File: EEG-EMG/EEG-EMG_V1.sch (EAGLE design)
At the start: 1 part

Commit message: Added 4 input stage amplifiers- AD8237
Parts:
- added BAT1: 2032, SMTU-2032-1:2032
- added C1, C10, C11, C2, C4, C5, C7, C8: 0.1uF, SparkFun-Capacitors:CAP0805
- added C12, C3, C6, C9: 1uF, SparkFun-Capacitors:CAP0805
- added IA_1, IA_2, IA_4: AD8237, wts_transmitter:AD8237
- added JP1: (no value), jumper:JP2W
- added JP2: (no value), jumper:JP2Q
- added R1, R10, R4, R7: 100k, SparkFun-Passives:RESISTOR0805-RES
- added R11, R2, R5, R8: 2k, SparkFun-Passives:RESISTOR0805-RES
- added R12, R3, R6, R9: 1k, SparkFun-Passives:RESISTOR0805-RES
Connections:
- new net EEG1+: IA_1.IN+, JP1.1
- new net EEG2+: IA_2.IN+, JP1.2
- new net EMG1+: IA_3.IN+, JP2.1
- new net EMG1-: IA_3.IN-, JP2.2
- new net EMG2+: IA_4.IN+, JP2.3
- new net EMG2-: IA_4.IN-, JP2.4
- new net GND: BAT1.-, C1.1, C10.1, C11.1, C12.2, C2.1, C3.2, C4.1, C5.1, C6.2, C7.1, C8.1, C9.2, IA_1.-VS, IA_2.-VS, IA_3.-VS, IA_4.-VS
- new net N$1: IA_1.VOUT, R1.1, R3.1
- new net N$10: IA_4.VOUT, R10.1, R12.1
- new net N$11: IA_4.FB, R10.2, R11.2
- new net N$12: C12.1, R12.2
- new net N$2: IA_1.FB, R1.2, R2.2
- new net N$3: C3.1, R3.2
- new net N$4: IA_2.VOUT, R4.1, R6.1
- new net N$5: IA_2.FB, R4.2, R5.2
- new net N$6: C6.1, R6.2
- new net N$7: IA_3.VOUT, R7.1, R9.1
- new net N$8: IA_3.FB, R7.2, R8.2
- new net N$9: C9.1, R9.2
- new net REF: IA_1.IN-, IA_2.IN-, JP1.3
- new net VAA: BAT1.+, C1.2, C10.2, C11.2, C2.2, C4.2, C5.2, C7.2, C8.2, IA_1.+VS, IA_1.BW, IA_2.+VS, IA_2.BW, IA_3.+VS, IA_3.BW, IA_4.+VS, IA_4.BW
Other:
- moved on the sheet: IA_3

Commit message: Added MCP6v31U
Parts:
- added C13, C14, C15, C16: 3.3uF, SparkFun-Capacitors:CAP0805
- added IC1, IC2, IC3, IC4: MCP6V31, linear:MCP601OT
- added R13, R14, R15, R16, R18, R19, R22, R23: 1M, SparkFun-Passives:RESISTOR0805-RES
- added R17, R20, R21, R24: 500k, SparkFun-Passives:RESISTOR0805-RES
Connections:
- new net N$13: C13.1, IC1.-IN, R14.2
- new net N$14: C13.2, IC1.OUT, R13.2
- new net N$16: C14.1, IC2.-IN, R15.1, R16.2
- new net N$17: C14.2, IC2.OUT, R15.2
- new net N$19: C15.1, IC3.-IN, R18.1, R19.2
- new net N$20: C15.2, IC3.OUT, R18.2
- new net N$22: C16.1, IC4.-IN, R23.2
- new net N$23: C16.2, IC4.OUT, R22.2
- net GND: now also IC1.V+, IC2.V+, IC3.V+, IC4.V+
- net N$2: now also R14.1
- net N$5: now also R16.1
- net N$8: now also R19.1
- net VAA: now also IC1.V-, IC2.V-, IC3.V-, IC4.V-

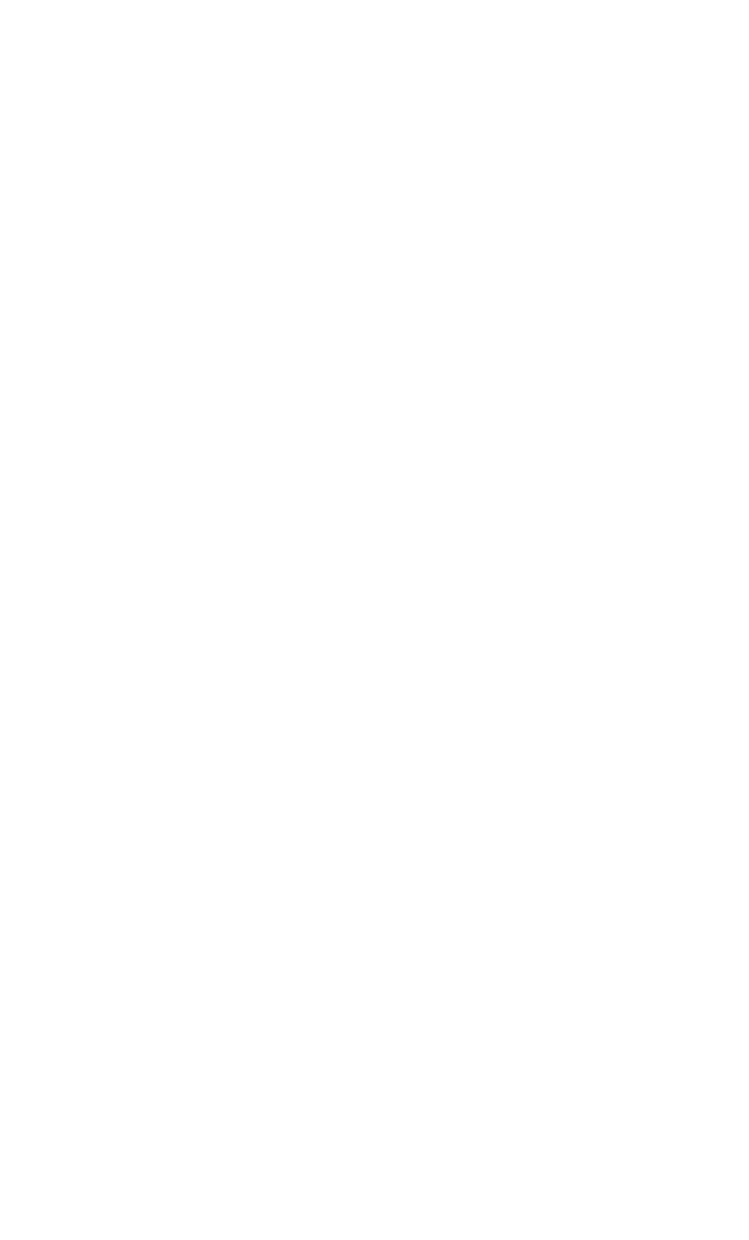
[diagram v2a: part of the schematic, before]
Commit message: Imported Components MCP3912 & LM7332MA
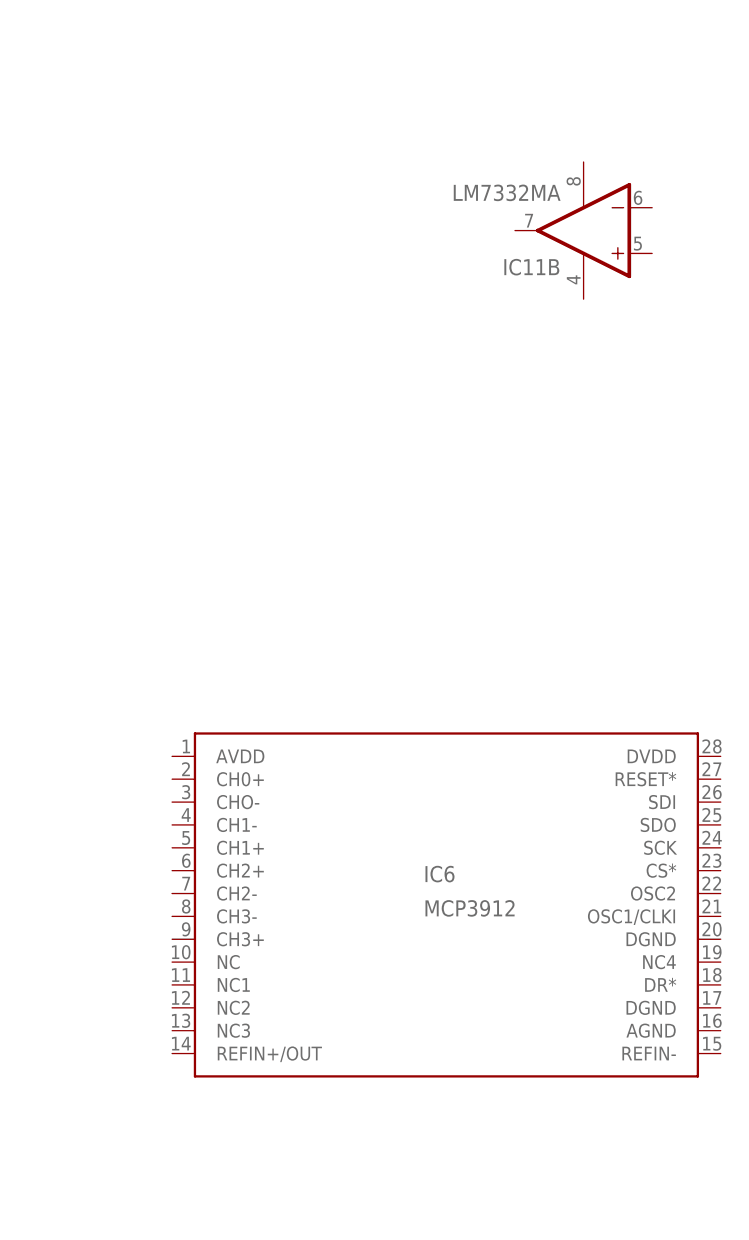
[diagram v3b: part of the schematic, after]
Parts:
- added IC11: LM7332MA, linear:LM1458D
- added IC6: MCP3912, SensorCape:MCP3912
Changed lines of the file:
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@@
 <part name="GND13" library="SparkFun-Aesthetics" deviceset="GND" device=""/>
 <part name="SUPPLY9" library="SparkFun-Aesthetics" deviceset="3.3V" device=""/>
+<part name="IC11" library="linear" deviceset="*1458" device="D" technology="LM" value="LM7332MA"/>
+<part name="IC6" library="SensorCape" deviceset="MCP3912" device=""/>
 </parts>
 <sheets>
@@
 </instance>
 <instance part="SUPPLY9" gate="G$1" x="647.7" y="-416.56" rot="R270"/>
+<instance part="IC11" gate="B" x="762" y="-149.86" rot="R180"/>
+<instance part="IC11" gate="P" x="762" y="-149.86"/>
+<instance part="IC6" gate="G$1" x="746.76" y="-223.52"/>
 </instances>
 <busses>

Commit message: Completed connections to all 4 Instrumentation Amplifiers
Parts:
- added C17: 0.1uF, SparkFun-Capacitors:CAP0805
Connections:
- new net N$15: C17.1, IC11B.+IN, IC6.REFIN+/OUT
- new net N$18: IC11B.-IN, IC11B.OUT, IC6.CH1-, IC6.CH2-, IC6.CH3-, IC6.CHO-, R11.1, R17.1, R2.1, R20.1, R21.1, R24.1, R5.1, R8.1
- new net N$21: IC2.+IN, R17.2
- new net N$24: IC3.+IN, R20.2
- new net N$25: IC1.+IN, R21.2
- new net N$26: IC4.+IN, R24.2
- net GND: now also C17.2, IC11P.V-
- net N$12: now also IC6.CH3+
- net N$14: now also IA_1.REF
- net N$17: now also IA_2.REF
- net N$20: now also IA_3.REF
- net N$23: now also IA_4.REF
- net N$3: now also IC6.CH0+
- net N$6: now also IC6.CH1+
- net VAA: now also IC11P.V+
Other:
- moved on the sheet: IC6

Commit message: Completed connections to MCP3912
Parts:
- added BAT2: 2032, SMTU-2032-1:2032
- added BATT: M02POLAR_LOCK, SparkFun-Connectors:M02POLAR_LOCK
- added C18, C45: 0.1uF, SparkFun-Capacitors:CAP0805
- added C19, C20: 18uF, SparkFun-Capacitors:CAP0805
- added C21, C22, C25, C28, C33, C37, C38: 0.1uF, resistor:C-EUC1206
- added C23, C31, C43: 10uF, resistor:C-EUC1206
- added C24, C26, C27, C39, C40: 1uF, resistor:C-EUC1206
- added C29, C30, C41, C42: 18pF, resistor:C-EUC1206
- added C32: 100nF, resistor:C-EUC1206
- added C34, C35: 4.7uF, resistor:C-EUC1206
- added C36, C44: 47 uF, resistor:C-EUC1206
- added CONN1: ANALOG, adafruit:PINHD-1X6B
- added CONN2: DIGITAL, adafruit:PINHD-1X8BIG
- added CONN3: DIGITAL, adafruit:PINHD-1X10
- added CONN4: DIGITAL RASTER, adafruit:PINHD-1X10
- added CONN5: POWER, adafruit:PINHD-1X6B
- added D13, D13_2, RX, RX1, TX, TX1: Green, SparkFun-LED:LED1206
- added D3: B330A, aaron_discrete:B330A
- added D4: POWER, SparkFun-LED:LED1206
- added F1, F2: 1206L, microbuilder:PTC1206_L
- added FET1, FET3: TR, aaron_discrete:IRLML2502TR
- added JP3, JP4: ISP, SparkFun:AVR_SPI_PRG_6PTH
- added JP5, JP6: (no value), SparkFun-Connectors:M03X22X3_SILK_SM
- added L1: Ferrite, wuerth-elektronik:WE-CBF_1206W
- added L2: BRL3225T3R3M, resistor:L-EUL3225P
- added MINIUSB, MINIUSB1: MINI-USB-SCHIELD-32005-201, con-cypressindustries:MINI-USB-SCHIELD-32005-201
- added MUX: 74HC4051, SparkFun-AnalogIC:74HC4051_MUX
- added Q1, Q6, Q7: CSM-3X-CRYSTALCSM-3X, fmc:CSM-3X-CRYSTALCSM-3X
- added Q2, Q3, Q4, Q5: QRE1113, aaron_discrete:QRE1113
- added R25, R31, R33, R35, R37, R39, R47, R48: 10K, resistor:R-EU_R1206
- added R26, R29, R30, R43, R44, R45, R51: 1K, resistor:R-EU_R1206
- added R27, R28, R50, R52: 22, resistor:R-EU_R1206
- added R32, R34, R36, R38, R40, R46: 100, resistor:R-EU_R1206
- added R41: 470, resistor:R-EU_R1206
- added R42: 2K, resistor:R-EU_R1206
- added R49: 3.09k, resistor:R-EU_R1206
- added R53, R54: 2.2K, resistor:R-EU_R1206
- added S1, S2: Reset, SparkFun:TAC_SWITCHSMD
- added SERVO1(USONIC): USONIC, pinhead:PINHD-1X3
- added SERVO2(GRIP): GRIPPER, pinhead:PINHD-1X3
- added SERVO3(GRIPROT): ROTATE, pinhead:PINHD-1X3
- added SER_CPU2: SER2, pinhead:PINHD-1X2
- added SHIFT1, SHIFT2: 74HC595D, 74xx-eu:74HC595D
- added STEPPER_DRIVER: ULN2803, SparkFun-PowerIC:ULN2803SOICW
- added SW1: (no value), switch:SPDT
- added U$10: PNA460XM, adafruit:PNA460XM
- added U$2: 1.8TFT+SD, muzy_robot:1.8TFT+SD
- added U$3: GY-521, muzy_robot:GY-521
- added U$4: HMC5883L, muzy_robot:HMC5883L
- added U$5: NRF24L01+, muzy_robot:NRF24L01+
- added U1: USER, adafruit:ATMEGA32U4-AU
- added U2: BRAIN, adafruit:ATMEGA32U4-AU
- added U3: LP2985, SparkFun:V_REG_LDOSMD
- added U4: MCP1650, aaron_ic:MCP1650
- added U5: MCP73831, SparkFun:MCP73831SMD
- added ULTRASONIC: (no value), pinhead:PINHD-1X4
- added X1, X2: 05-JST-B5B-XH-A, con-jst-xh:05-JST-B5B-XH-A
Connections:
- removed net VAA: BAT1.+, C1.2, C10.2, C11.2, C2.2, C4.2, C5.2, C7.2, C8.2, IA_1.+VS, IA_1.BW, IA_2.+VS, IA_2.BW, IA_3.+VS, IA_3.BW, IA_4.+VS, IA_4.BW, IC1.V-, IC11P.V+, IC2.V-, IC3.V-, IC4.V-
- new net 2D+: R50.1, U2.D+
- new net 2D-: R52.1, U2.D-
- new net 2D13: R43.1, U2.PC7(ICP3/CLK0/OC4A)
- new net 2MISO: JP4.1, U$2.SD_MISO, U$5.MISO, U2.PB3(PDO/MISO)
- new net 2MOSI: JP4.4, SHIFT1A.SER, U$2.SDA, U$2.SD_MOSI, U$5.MOSI, U2.PB2(PDI/MISO)
- new net 2RESET: JP4.5, R47.1, S1.3, S1.4, U2./RESET
- new net 2RXLED: R44.1, U2.PB0(SS)
- new net 2SCK: JP4.3, SHIFT1A.SCK, SHIFT2A.SCK, U$2.SCK, U$2.SD_SCK, U$5.SCK, U2.PB1(SCK)
- new net 2TXLED: R45.1, U2.PD5(XCK/CTS)
- new net 2XTAL3: C42.1, Q6.2, U2.XTAL2
- new net 2XTAL4: C41.1, Q6.1, U2.XTAL1
- new net 3.3V: C31.1, C32.1, CONN5.2, U$2.LED, U$5.VCC, U3.OUT
- new net A0: CONN1.1, U1.PF7(ADC7(TDI)
- new net A1: CONN1.2, U1.PF6(ADC6/TDO)
- new net A2: CONN1.3, U1.PF5(ADC5/TMS)
- new net A3: CONN1.4, U1.PF4(ADC4/TCK)
- new net A4: CONN1.5, U1.PF1(ADC1)
- new net A5: CONN1.6, U1.PF0(ADC0)
- new net AREF: C22.2, C38.2, CONN3.8, CONN4.8, U1.AREF, U2.AREF
- new net AVCC: C25.1, C28.1, L1.2, U1.AVCC, U1.AVCC1, U2.AVCC, U2.AVCC1
- new net BATT_OUT: C44.1, D3.C, R46.2, R49.2, SW1.1
- new net D+: R27.1, U1.D+
- new net D-: R28.1, U1.D-
- new net D10: CONN3.3, CONN4.3, U1.PB6(OC1B/OC4B/ADC13)
- new net D11: CONN3.4, CONN4.4, U1.PB7(OC0A/OC1C/RTS)
- new net D12: CONN3.5, CONN4.5, U1.PD6(T1/OC4D/ADC9)
- new net D13: CONN3.6, CONN4.6, R26.1, U1.PC7(ICP3/CLK0/OC4A)
- new net D4: CONN2.5, U1.PD4(ICP1/ADC8)
- new net D5: CONN2.6, U1.PC6(OC1A)
- new net D6: CONN2.7, U1.PD7(OC4D/ADC10/T0)
- new net D7: CONN2.8, U1.PE6
- new net D8: CONN3.1, CONN4.1, U1.PB4(ADC11)
- new net D9: CONN3.2, CONN4.2, U1.PB5(OC1A/OC4B/ADC12)
- new net ECHO: U2.PF6(ADC6/TDO), ULTRASONIC.2
- new net IR: U$10.OUT, U2.PD4(ICP1/ADC8)
- new net IRA: JP6.1, MUX.A
- new net IRB: JP6.3, MUX.B
- new net IRC: JP6.5, MUX.C
- new net IR_GND: JP6.6, MUX.INH, MUX.VEE, MUX.VSS, Q2.E, Q2.K, Q3.E, Q3.K, Q4.E, Q4.K, Q5.E, Q5.K
- new net IR_OUT: JP6.4, MUX.IO
- new net IR_VCC: JP6.2, MUX.VDD, R32.2, R33.2, R34.2, R35.2, R36.2, R37.2, R38.2, R39.2
- new net MISO: JP3.1, U1.PB3(PDO/MISO)
- new net MOSI: JP3.4, U1.PB2(PDI/MISO)
- new net MUX0: MUX.IO0, Q2.C, R33.1
- new net MUX1: MUX.IO1, Q3.C, R35.1
- new net MUX2: MUX.IO2, Q4.C, R37.1
- new net MUX3: MUX.IO3, Q5.C, R39.1
- new net MUX_OUT: JP5.4, U2.PF0(ADC0)
- new net N$134: C19.2, IC6.OSC1/CLKI, Q7.1
- new net N$135: C20.2, IC6.OSC2, Q7.2
- new net N$136: D13.A, R26.2
- new net N$137: R31.1, U1.PE2(HWB)
- new net N$138: F2.1, MINIUSBG$1.1
- new net N$139: R30.2, TX.C
- new net N$140: R29.2, RX.C
- new net N$141: MINIUSBG$1.2, R28.2
- new net N$142: MINIUSBG$1.3, R27.2
- new net N$143: Q2.A, R32.1
- new net N$144: Q3.A, R34.1
- new net N$145: Q4.A, R36.1
- new net N$146: Q5.A, R38.1
- new net N$147: FET1.G, R40.2
- new net N$148: R49.1, R51.2, U4.FB
- new net N$149: C33.1, R46.1, U4./SHDN, U4.CS, U4.VIN
- new net N$150: FET3.G, U4.EXT
- new net N$151: D3.A, FET3.D, L2.2
- new net N$152: R42.1, U5.PROG
- new net N$153: R41.1, U5.STAT
- new net N$154: D4.C, R41.2
- new net N$155: STEPPER_DRIVER.11, X2-4.1
- new net N$156: STEPPER_DRIVER.12, X2-3.1
- new net N$157: STEPPER_DRIVER.13, X2-2.1
- new net N$158: STEPPER_DRIVER.14, X2-1.1
- new net N$159: STEPPER_DRIVER.15, X1-4.1
- new net N$160: STEPPER_DRIVER.16, X1-3.1
- new net N$161: STEPPER_DRIVER.17, X1-2.1
- new net N$162: STEPPER_DRIVER.18, X1-1.1
- new net N$163: D13_2.A, R43.2
- new net N$164: R45.2, TX1.C
- new net N$165: R44.2, RX1.C
- new net N$166: R48.1, U2.PE2(HWB)
- new net N$167: F1.1, MINIUSB1G$1.1
- new net N$168: MINIUSB1G$1.2, R52.2
- new net N$169: MINIUSB1G$1.3, R50.2
- new net N$170: SER_CPU2.1, U2.PD3(INT3/TXD1)
- new net N$171: SER_CPU2.2, U2.PD2(INT2/RXD1)
- new net N$172: C39.1, U2.UCAP
- new net N$173: C26.1, U1.UCAP
- new net N$174: JP5.1, SHIFT2A.QA
- new net N$175: JP5.3, SHIFT2A.QB
- new net N$176: JP5.5, SHIFT2A.QC
- new net N$177: FET1.D, JP5.6
- new net NRF_CE: U$5.CE, U2.PB5(OC1A/OC4B/ADC12)
- new net NRF_CSN: U$5.CSN, U2.PB6(OC1B/OC4B/ADC13)
- new net NRF_IRQ: U$5.IRQ, U2.PE6
- new net RESET: CONN5.1, JP3.5, R25.1, S2.3, S2.4, U1./RESET
- new net RX-I: CONN2.1, U1.PD2(INT2/RXD1)
- new net RXLED: R29.1, U1.PB0(SS)
- new net S1: SHIFT1A.QA, STEPPER_DRIVER.8
- new net S1OVERFLOW1: SHIFT1A.QH*, SHIFT2A.SER
- new net S2: SHIFT1A.QB, STEPPER_DRIVER.7
- new net S2O4: R40.1, SHIFT2A.QD
- new net S3: SHIFT1A.QC, STEPPER_DRIVER.6
- new net S4: SHIFT1A.QD, STEPPER_DRIVER.5
- new net S5: SHIFT1A.QE, STEPPER_DRIVER.4
- new net S6: SHIFT1A.QF, STEPPER_DRIVER.3
- new net S7: SHIFT1A.QG, STEPPER_DRIVER.2
- new net S8: SHIFT1A.QH, STEPPER_DRIVER.1
- new net SCK: JP3.3, U1.PB1(SCK)
- new net SCL: CONN2.4, CONN3.10, CONN4.10, R53.1, U$3.SCL, U$4.SCL, U1.PD0(INT0/OC0B), U2.PD0(INT0/OC0B)
- new net SDA: CONN2.3, CONN3.9, CONN4.9, R54.1, U$3.SDA, U$4.SDA, U1.PD1(INT1/SDA), U2.PD1(INT1/SDA)
- new net SD_CS: U$2.SD_CS, U2.PB4(ADC11)
- new net SHIFT_RCK: SHIFT1A.RCK, SHIFT2A.RCK, U2.PD6(T1/OC4D/ADC9)
- new net S_GRIP: SERVO2(GRIP).3, U2.PD7(OC4D/ADC10/T0)
- new net S_GRIPROT: SERVO3(GRIPROT).3, U2.PB7(OC0A/OC1C/RTS)
- new net S_USONIC: SERVO1(USONIC).3, U2.PC6(OC1A)
- new net TFT_CS: U$2.CS, U2.PF1(ADC1)
- new net TFT_DC: U$2.AD, U2.PF5(ADC5/TMS)
- new net TFT_RST: U$2.RESET, U2.PF4(ADC4/TCK)
- new net TRIG: U2.PF7(ADC7(TDI), ULTRASONIC.3
- new net TX-O: CONN2.2, U1.PD3(INT3/TXD1)
- new net TXLED: R30.1, U1.PD5(XCK/CTS)
- new net USB_VIN: C23.1, C34.1, C43.1, D4.A, F1.2, F2.2, SW1.3, U5.VIN
- new net VBATT: BATT.2, C35.1, C36.2, L2.1, U5.VBAT
- new net VCC: C21.1, C24.1, C27.1, C37.1, C40.1, CONN5.3, JP3.2, JP4.2, JP5.2, L1.1, R25.2, R47.2, R53.2, R54.2, RX.A, RX1.A, SERVO1(USONIC).2, SERVO2(GRIP).2, SERVO3(GRIPROT).2, SHIFT1A.SCL, SHIFT1P.VCC, SHIFT2A.SCL, SHIFT2P.VCC, STEPPER_DRIVER.10, SW1.2, TX.A, TX1.A, U$10.VCC, U$2.VCC, U$3.VCC, U$4.VCC, U1.UVCC, U1.VBUS, U1.VCC, U1.VCC1, U2.UVCC, U2.VBUS, U2.VCC, U2.VCC1, U3.EN, U3.IN, ULTRASONIC.4, X1-5.1, X2-5.1
- new net VDD: BAT1.+, BAT2.+, C1.2, C10.2, C11.2, C18.2, C2.2, C4.2, C45.2, C5.2, C7.2, C8.2, IA_1.+VS, IA_1.BW, IA_2.+VS, IA_2.BW, IA_3.+VS, IA_3.BW, IA_4.+VS, IA_4.BW, IC1.V-, IC11P.V+, IC2.V-, IC3.V-, IC4.V-, IC6.AVDD, IC6.DVDD
- new net XTAL3: C30.1, Q1.2, U1.XTAL2
- new net XTAL4: C29.1, Q1.1, U1.XTAL1
- net GND: now also BAT2.-, BATT.1, C18.1, C19.1, C20.1, C21.2, C22.1, C23.2, C24.2, C25.2, C26.2, C27.2, C28.2, C29.2, C30.2, C31.2, C32.2, C33.2, C34.2, C35.2, C36.1, C37.2, C38.1, C39.2, C40.2, C41.2, C42.2, C43.2, C44.2, C45.1, CONN3.7, CONN4.7, CONN5.4, CONN5.5, D13.C, D13_2.C, FET1.S, FET3.S, IC6.AGND, IC6.DGND, IC6.DGND@1, IC6.NC, IC6.NC1, IC6.NC2, IC6.NC3, IC6.NC4, IC6.REFIN-, JP3.6, JP4.6, MINIUSB1G$1.5, MINIUSB1S.S1, MINIUSB1S.S2, MINIUSB1S.S3, MINIUSB1S.S4, MINIUSBG$1.5, MINIUSBS.S1, MINIUSBS.S2, MINIUSBS.S3, MINIUSBS.S4, R31.2, R42.2, R48.2, R51.1, S1.1, S1.2, S2.1, S2.2, SERVO1(USONIC).1, SERVO2(GRIP).1, SERVO3(GRIPROT).1, SHIFT1A.G, SHIFT1P.GND, SHIFT2A.G, SHIFT2P.GND, STEPPER_DRIVER.9, U$10.GND, U$2.GND, U$3.GND, U$4.GND, U$5.GND, U1.GND, U1.GND1, U1.GND2, U1.GND3, U1.UGND, U2.GND, U2.GND1, U2.GND2, U2.GND3, U2.UGND, U3.GND, U4.GND, U5.VSS, ULTRASONIC.1
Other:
- note added: "1.8" SPI Display (128*160px)"
- note added: "3.3V LDO"
- note added: "38KHz with digital output"
- note added: "Accelerometer and Gyroscope (GY-521, optional, plug-in module)"
- note added: "Analog Supply (CPU 1 and CPU 2)"
- note added: "Arduino Breakouts (CPU 1)"
- note added: "CPU 1 (ATMEGA32U4)"
- note added: "CPU 2 (ATMEGA32U4)"
- note added: "Compass (optional, plug-in module)"
- note added: "Edubot V.0.12 by Sebastian Muszytowski <muzy@muzy.eu>"
- note added: "GRIP mechanism servo"
- note added: "HC-SR04"
- note added: "HMC5883L"
- note added: "I2C Pullup"
- note added: "IR Reciever"
- note added: "ISP (CPU1)"
- note added: "ISP (CPU2)"
- note added: "Infrared Sensors (for Line Following)"
- note added: "Left Motor"
- note added: "LiPo Charge Circuit (PROG = 2K = 500mA)"
- note added: "MPU 6050"
- note added: "NO SUPPORT FOR VIN DUE TO MISSING REGULATOR. EVERYTHING ABOVE 5.5V DAMAGES THE BOARD!"
- note added: "NRF24L01 Breakout"
- note added: "Power Selector"
- note added: "ROTATE mechanism servo"
- note added: "Reset (CPU1)"
- note added: "Reset (CPU2)"
- note added: "Right Motor"
- note added: "Servo 1 (Ultrasonic)"
- note added: "Servo 2 and 3 (Gripper)"
- note added: "Shift Register and Mulitplexer (CPU 2)"
- note added: "Status LEDs (CPU1)"
- note added: "Status LEDs (CPU2)"
- note added: "Step-Up-Converter (2.8 to 4.2Volt to 5V @ 1A)"
- note added: "USB (CPU1)"
- note added: "USB (CPU2)"
- note added: "Ultrasonic distance sensor"
- note added: "based on Vinciduino Schematic and ATmega32U4 data sheet; Arduino Leonardo compatible with Headers The user mainly programs this microcontroller."
- note added: "based on Vinciduino Schematic and ATmega32U4 data sheet; Arduino Leonardo compatible without Headers This microcontroller serves as the "brain" interfacing internal components."
- note added: "for moving the Ultrasonic distance sensor to scan the environment"
- note added: "licensed under CC-BY-SA 3.0, based on the beautiful Vinciduino (vinciduino.org), inspired by Sparki (arcbotics.com), made with the lovely Arduino Leonardo in mind (arduino.cc)"
- note added: "on 2x4pin header pinout"
- note added: "optional, only populate when no other component provides pullup resistors! Values may vary (from 2.2K to 10K)"
- note added: "with SD Card Adapter (optional, plug-in module)"

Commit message: Added Bluetooth Module BGM111
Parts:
- removed BATT: M02POLAR_LOCK, SparkFun-Connectors:M02POLAR_LOCK
- removed C28, C33, C37, C38: 0.1uF, resistor:C-EUC1206
- removed C29, C30, C41, C42: 18pF, resistor:C-EUC1206
- removed C31, C43: 10uF, resistor:C-EUC1206
- removed C32: 100nF, resistor:C-EUC1206
- removed C34, C35: 4.7uF, resistor:C-EUC1206
- removed C36, C44: 47 uF, resistor:C-EUC1206
- removed C39, C40: 1uF, resistor:C-EUC1206
- removed CONN1: ANALOG, adafruit:PINHD-1X6B
- removed CONN2: DIGITAL, adafruit:PINHD-1X8BIG
- removed CONN3: DIGITAL, adafruit:PINHD-1X10
- removed CONN4: DIGITAL RASTER, adafruit:PINHD-1X10
- removed CONN5: POWER, adafruit:PINHD-1X6B
- removed D13, D13_2, RX, RX1, TX, TX1: Green, SparkFun-LED:LED1206
- removed D3: B330A, aaron_discrete:B330A
- removed D4: POWER, SparkFun-LED:LED1206
- removed F1, F2: 1206L, microbuilder:PTC1206_L
- removed FET1, FET3: TR, aaron_discrete:IRLML2502TR
- removed JP5, JP6: (no value), SparkFun-Connectors:M03X22X3_SILK_SM
- removed L1: Ferrite, wuerth-elektronik:WE-CBF_1206W
- removed L2: BRL3225T3R3M, resistor:L-EUL3225P
- removed MINIUSB, MINIUSB1: MINI-USB-SCHIELD-32005-201, con-cypressindustries:MINI-USB-SCHIELD-32005-201
- removed MUX: 74HC4051, SparkFun-AnalogIC:74HC4051_MUX
- removed Q1, Q6: CSM-3X-CRYSTALCSM-3X, fmc:CSM-3X-CRYSTALCSM-3X
- removed Q2, Q3, Q4, Q5: QRE1113, aaron_discrete:QRE1113
- removed R43, R44, R45, R51: 1K, resistor:R-EU_R1206
- removed R46: 100, resistor:R-EU_R1206
- removed R47, R48: 10K, resistor:R-EU_R1206
- removed R49: 3.09k, resistor:R-EU_R1206
- removed R50, R52: 22, resistor:R-EU_R1206
- removed R53, R54: 2.2K, resistor:R-EU_R1206
- removed S1, S2: Reset, SparkFun:TAC_SWITCHSMD
- removed SERVO1(USONIC): USONIC, pinhead:PINHD-1X3
- removed SERVO2(GRIP): GRIPPER, pinhead:PINHD-1X3
- removed SERVO3(GRIPROT): ROTATE, pinhead:PINHD-1X3
- removed SER_CPU2: SER2, pinhead:PINHD-1X2
- removed SHIFT1, SHIFT2: 74HC595D, 74xx-eu:74HC595D
- removed STEPPER_DRIVER: ULN2803, SparkFun-PowerIC:ULN2803SOICW
- removed SW1: (no value), switch:SPDT
- removed U$10: PNA460XM, adafruit:PNA460XM
- removed U$2: 1.8TFT+SD, muzy_robot:1.8TFT+SD
- removed U$3: GY-521, muzy_robot:GY-521
- removed U$4: HMC5883L, muzy_robot:HMC5883L
- removed U$5: NRF24L01+, muzy_robot:NRF24L01+
- removed U3: LP2985, SparkFun:V_REG_LDOSMD
- removed U5: MCP73831, SparkFun:MCP73831SMD
- removed ULTRASONIC: (no value), pinhead:PINHD-1X4
- removed X1, X2: 05-JST-B5B-XH-A, con-jst-xh:05-JST-B5B-XH-A
- added BAT3: 2032, SMTU-2032-1:2032
- added J1, J2: (no value), tag-connect:TC2030-MCP-NL
- added LOGO3: OSHW-LOGOS, SparkFun-Aesthetics:OSHW-LOGOS
- C21: value 0.1uF -> 1nF; device resistor:C-EUC1206 -> SparkFun-Passives:CAP0603-CAP
- C22: value 0.1uF -> 0.1uf; device resistor:C-EUC1206 -> SparkFun-Passives:CAP0603-CAP
- C23: value 10uF -> 0.1uF; device resistor:C-EUC1206 -> SparkFun-Passives:CAP0603-CAP
- C24: value 1uF -> 0.33uF; device resistor:C-EUC1206 -> SparkFun-Passives:CAP0805
- C25: value 0.1uF -> 0.33uF; device resistor:C-EUC1206 -> SparkFun-Passives:CAP0805
- C26: value 1uF -> 1.5nF; device resistor:C-EUC1206 -> SparkFun-Passives:CAP0603-CAP
- C27: value 1uF -> 10nF; device resistor:C-EUC1206 -> SparkFun-Passives:CAP0603-CAP
- JP3, JP4: value ISP -> SEWTAP2; device SparkFun:AVR_SPI_PRG_6PTH -> LilyPad-Wearables:SEWTAP2
- R25: value 10K -> 180k; device resistor:R-EU_R1206 -> SparkFun-Passives:RESISTOR0603-RES
- R26: value 1K -> 180k; device resistor:R-EU_R1206 -> SparkFun-Passives:RESISTOR0603-RES
- R27: value 22 -> 1M; device resistor:R-EU_R1206 -> SparkFun-Passives:RESISTOR0603-RES
- R28: value 22 -> 10M; device resistor:R-EU_R1206 -> SparkFun-Passives:RESISTOR0603-RES
- R29: value 1K -> 10M; device resistor:R-EU_R1206 -> SparkFun-Passives:RESISTOR0603-RES
- R30: value 1K -> 1M; device resistor:R-EU_R1206 -> SparkFun-Passives:RESISTOR0603-RES
- R31: value 10K -> 100k; device resistor:R-EU_R1206 -> SparkFun-Passives:RESISTOR0603-RES
- R32, R36: value 100 -> 10M; device resistor:R-EU_R1206 -> SparkFun-Passives:RESISTOR0603-RES
- R33, R35: value 10K -> 10M; device resistor:R-EU_R1206 -> SparkFun-Passives:RESISTOR0603-RES
- R34: value 100 -> 1.4M; device resistor:R-EU_R1206 -> SparkFun-Passives:RESISTOR0603-RES
- R37: value 10K -> 1M; device resistor:R-EU_R1206 -> SparkFun-Passives:RESISTOR0603-RES
- R38: value 100 -> 360k; device resistor:R-EU_R1206 -> SparkFun-Passives:RESISTOR0603-RES
- R39: value 10K -> 0; device resistor:R-EU_R1206 -> SparkFun-Resistors:0OHM1/10W5%(0603)
- R40: value 100 -> DNP; device resistor:R-EU_R1206 -> SparkFun-Resistors:0OHM1/10W5%(0603)
- R41: value 470 -> 0; device resistor:R-EU_R1206 -> SparkFun-Resistors:0OHM1/10W5%(0603)
- R42: value 2K -> DNP; device resistor:R-EU_R1206 -> SparkFun-Resistors:0OHM1/10W5%(0603)
- U1: value USER -> AD8232; device adafruit:ATMEGA32U4-AU -> AD8232:AD8232
- U2: value BRAIN -> BGM111-VISUAL-A; device adafruit:ATMEGA32U4-AU -> sf-bluegiga:BGM111-VISUAL-A
- U4: value MCP1650 -> BGM111-VISUAL-A; device aaron_ic:MCP1650 -> sf-bluegiga:BGM111-VISUAL-A
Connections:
- removed net 2D+: R50.1, U2.D+
- removed net 2D-: R52.1, U2.D-
- removed net 2D13: R43.1, U2.PC7(ICP3/CLK0/OC4A)
- removed net 2MISO: JP4.1, U$2.SD_MISO, U$5.MISO, U2.PB3(PDO/MISO)
- removed net 2MOSI: JP4.4, SHIFT1A.SER, U$2.SDA, U$2.SD_MOSI, U$5.MOSI, U2.PB2(PDI/MISO)
- removed net 2RESET: JP4.5, R47.1, S1.3, S1.4, U2./RESET
- removed net 2RXLED: R44.1, U2.PB0(SS)
- removed net 2SCK: JP4.3, SHIFT1A.SCK, SHIFT2A.SCK, U$2.SCK, U$2.SD_SCK, U$5.SCK, U2.PB1(SCK)
- removed net 2TXLED: R45.1, U2.PD5(XCK/CTS)
- removed net 2XTAL3: C42.1, Q6.2, U2.XTAL2
- removed net 2XTAL4: C41.1, Q6.1, U2.XTAL1
- removed net A0: CONN1.1, U1.PF7(ADC7(TDI)
- removed net A1: CONN1.2, U1.PF6(ADC6/TDO)
- removed net A2: CONN1.3, U1.PF5(ADC5/TMS)
- removed net A3: CONN1.4, U1.PF4(ADC4/TCK)
- removed net A4: CONN1.5, U1.PF1(ADC1)
- removed net A5: CONN1.6, U1.PF0(ADC0)
- removed net AREF: C22.2, C38.2, CONN3.8, CONN4.8, U1.AREF, U2.AREF
- removed net AVCC: C25.1, C28.1, L1.2, U1.AVCC, U1.AVCC1, U2.AVCC, U2.AVCC1
- removed net BATT_OUT: C44.1, D3.C, R46.2, R49.2, SW1.1
- removed net D+: R27.1, U1.D+
- removed net D-: R28.1, U1.D-
- removed net D10: CONN3.3, CONN4.3, U1.PB6(OC1B/OC4B/ADC13)
- removed net D11: CONN3.4, CONN4.4, U1.PB7(OC0A/OC1C/RTS)
- removed net D12: CONN3.5, CONN4.5, U1.PD6(T1/OC4D/ADC9)
- removed net D13: CONN3.6, CONN4.6, R26.1, U1.PC7(ICP3/CLK0/OC4A)
- removed net D4: CONN2.5, U1.PD4(ICP1/ADC8)
- removed net D5: CONN2.6, U1.PC6(OC1A)
- removed net D6: CONN2.7, U1.PD7(OC4D/ADC10/T0)
- removed net D7: CONN2.8, U1.PE6
- removed net D8: CONN3.1, CONN4.1, U1.PB4(ADC11)
- removed net D9: CONN3.2, CONN4.2, U1.PB5(OC1A/OC4B/ADC12)
- removed net ECHO: U2.PF6(ADC6/TDO), ULTRASONIC.2
- removed net IR: U$10.OUT, U2.PD4(ICP1/ADC8)
- removed net IRA: JP6.1, MUX.A
- removed net IRB: JP6.3, MUX.B
- removed net IRC: JP6.5, MUX.C
- removed net IR_GND: JP6.6, MUX.INH, MUX.VEE, MUX.VSS, Q2.E, Q2.K, Q3.E, Q3.K, Q4.E, Q4.K, Q5.E, Q5.K
- removed net IR_OUT: JP6.4, MUX.IO
- removed net IR_VCC: JP6.2, MUX.VDD, R32.2, R33.2, R34.2, R35.2, R36.2, R37.2, R38.2, R39.2
- removed net MISO: JP3.1, U1.PB3(PDO/MISO)
- removed net MOSI: JP3.4, U1.PB2(PDI/MISO)
- removed net MUX0: MUX.IO0, Q2.C, R33.1
- removed net MUX1: MUX.IO1, Q3.C, R35.1
- removed net MUX2: MUX.IO2, Q4.C, R37.1
- removed net MUX3: MUX.IO3, Q5.C, R39.1
- removed net MUX_OUT: JP5.4, U2.PF0(ADC0)
- removed net N$136: D13.A, R26.2
- removed net N$137: R31.1, U1.PE2(HWB)
- removed net N$138: F2.1, MINIUSBG$1.1
- removed net N$139: R30.2, TX.C
- removed net N$140: R29.2, RX.C
- removed net N$141: MINIUSBG$1.2, R28.2
- removed net N$142: MINIUSBG$1.3, R27.2
- removed net N$143: Q2.A, R32.1
- removed net N$144: Q3.A, R34.1
- removed net N$145: Q4.A, R36.1
- removed net N$146: Q5.A, R38.1
- removed net N$147: FET1.G, R40.2
- removed net N$148: R49.1, R51.2, U4.FB
- removed net N$149: C33.1, R46.1, U4./SHDN, U4.CS, U4.VIN
- removed net N$150: FET3.G, U4.EXT
- removed net N$151: D3.A, FET3.D, L2.2
- removed net N$152: R42.1, U5.PROG
- removed net N$153: R41.1, U5.STAT
- removed net N$154: D4.C, R41.2
- removed net N$155: STEPPER_DRIVER.11, X2-4.1
- removed net N$156: STEPPER_DRIVER.12, X2-3.1
- removed net N$157: STEPPER_DRIVER.13, X2-2.1
- removed net N$158: STEPPER_DRIVER.14, X2-1.1
- removed net N$159: STEPPER_DRIVER.15, X1-4.1
- removed net N$160: STEPPER_DRIVER.16, X1-3.1
- removed net N$161: STEPPER_DRIVER.17, X1-2.1
- removed net N$162: STEPPER_DRIVER.18, X1-1.1
- removed net N$163: D13_2.A, R43.2
- removed net N$164: R45.2, TX1.C
- removed net N$165: R44.2, RX1.C
- removed net N$166: R48.1, U2.PE2(HWB)
- removed net N$167: F1.1, MINIUSB1G$1.1
- removed net N$168: MINIUSB1G$1.2, R52.2
- removed net N$169: MINIUSB1G$1.3, R50.2
- removed net N$170: SER_CPU2.1, U2.PD3(INT3/TXD1)
- removed net N$171: SER_CPU2.2, U2.PD2(INT2/RXD1)
- removed net N$172: C39.1, U2.UCAP
- removed net N$173: C26.1, U1.UCAP
- removed net N$174: JP5.1, SHIFT2A.QA
- removed net N$175: JP5.3, SHIFT2A.QB
- removed net N$176: JP5.5, SHIFT2A.QC
- removed net N$177: FET1.D, JP5.6
- removed net NRF_CE: U$5.CE, U2.PB5(OC1A/OC4B/ADC12)
- removed net NRF_CSN: U$5.CSN, U2.PB6(OC1B/OC4B/ADC13)
- removed net NRF_IRQ: U$5.IRQ, U2.PE6
- removed net RESET: CONN5.1, JP3.5, R25.1, S2.3, S2.4, U1./RESET
- removed net RX-I: CONN2.1, U1.PD2(INT2/RXD1)
- removed net RXLED: R29.1, U1.PB0(SS)
- removed net S1: SHIFT1A.QA, STEPPER_DRIVER.8
- removed net S1OVERFLOW1: SHIFT1A.QH*, SHIFT2A.SER
- removed net S2: SHIFT1A.QB, STEPPER_DRIVER.7
- removed net S2O4: R40.1, SHIFT2A.QD
- removed net S3: SHIFT1A.QC, STEPPER_DRIVER.6
- removed net S4: SHIFT1A.QD, STEPPER_DRIVER.5
- removed net S5: SHIFT1A.QE, STEPPER_DRIVER.4
- removed net S6: SHIFT1A.QF, STEPPER_DRIVER.3
- removed net S7: SHIFT1A.QG, STEPPER_DRIVER.2
- removed net S8: SHIFT1A.QH, STEPPER_DRIVER.1
- removed net SCK: JP3.3, U1.PB1(SCK)
- removed net SCL: CONN2.4, CONN3.10, CONN4.10, R53.1, U$3.SCL, U$4.SCL, U1.PD0(INT0/OC0B), U2.PD0(INT0/OC0B)
- removed net SDA: CONN2.3, CONN3.9, CONN4.9, R54.1, U$3.SDA, U$4.SDA, U1.PD1(INT1/SDA), U2.PD1(INT1/SDA)
- removed net SD_CS: U$2.SD_CS, U2.PB4(ADC11)
- removed net SHIFT_RCK: SHIFT1A.RCK, SHIFT2A.RCK, U2.PD6(T1/OC4D/ADC9)
- removed net S_GRIP: SERVO2(GRIP).3, U2.PD7(OC4D/ADC10/T0)
- removed net S_GRIPROT: SERVO3(GRIPROT).3, U2.PB7(OC0A/OC1C/RTS)
- removed net S_USONIC: SERVO1(USONIC).3, U2.PC6(OC1A)
- removed net TFT_CS: U$2.CS, U2.PF1(ADC1)
- removed net TFT_DC: U$2.AD, U2.PF5(ADC5/TMS)
- removed net TFT_RST: U$2.RESET, U2.PF4(ADC4/TCK)
- removed net TRIG: U2.PF7(ADC7(TDI), ULTRASONIC.3
- removed net TX-O: CONN2.2, U1.PD3(INT3/TXD1)
- removed net TXLED: R30.1, U1.PD5(XCK/CTS)
- removed net USB_VIN: C23.1, C34.1, C43.1, D4.A, F1.2, F2.2, SW1.3, U5.VIN
- removed net VBATT: BATT.2, C35.1, C36.2, L2.1, U5.VBAT
- removed net VCC: C21.1, C24.1, C27.1, C37.1, C40.1, CONN5.3, JP3.2, JP4.2, JP5.2, L1.1, R25.2, R47.2, R53.2, R54.2, RX.A, RX1.A, SERVO1(USONIC).2, SERVO2(GRIP).2, SERVO3(GRIPROT).2, SHIFT1A.SCL, SHIFT1P.VCC, SHIFT2A.SCL, SHIFT2P.VCC, STEPPER_DRIVER.10, SW1.2, TX.A, TX1.A, U$10.VCC, U$2.VCC, U$3.VCC, U$4.VCC, U1.UVCC, U1.VBUS, U1.VCC, U1.VCC1, U2.UVCC, U2.VBUS, U2.VCC, U2.VCC1, U3.EN, U3.IN, ULTRASONIC.4, X1-5.1, X2-5.1
- removed net XTAL3: C30.1, Q1.2, U1.XTAL2
- removed net XTAL4: C29.1, Q1.1, U1.XTAL1
- new net LA: JP3.1, R25.1, R33.1
- new net LO+: U1.LO+
- new net LO-: U1.LO-
- new net N$100: C24.1, R34.2, R40.2, U1.SW
- new net N$101: C21.1, U1.RLDFB
- new net N$102: C26.2, R27.1, R37.1
- new net N$103: C21.2, R38.1, U1.RLD
- new net N$104: R35.1, R37.2, U1.IAOUT
- new net N$105: R32.2, R33.2, R39.2, R40.1
- new net N$106: R41.2, R42.1, U1.AC/!DC
- new net N$107: J1.VPP/MCLR, U4.RESET
- new net N$108: J1.ICSP_CLK/PGC, U4.PF0
- new net N$109: J1.ICSP_DAT/PGD, U4.PF1
- new net N$110: J2.VPP/MCLR, U2.RESET
- new net N$111: J2.ICSP_CLK/PGC, U2.PF0
- new net N$112: J2.ICSP_DAT/PGD, U2.PF1
- new net N$27: IC6.SDO, U2.PB11
- new net N$92: R25.2, U1.+IN
- new net N$93: R26.2, U1.-IN
- new net N$94: C27.2, R27.2, U1.OPAMP+
- new net N$95: C25.2, R28.1, U1.HPSENSE
- new net N$96: C22.1, R29.2, R36.2, U1.REFIN
- new net N$97: R30.2, R31.1, U1.OPAMP-
- new net N$98: C25.1, U1.HPDRIVE
- new net N$99: R28.2, R34.1, R35.2
- new net RA: JP4.1, R26.1, R32.1
- new net REFOUT: C24.2, C27.1, R31.2, U1.REFOUT
- new net RL: R38.2
- new net SDN: U1.!SDN
- new net SIGNAL_OUT: C26.1, R30.1, U1.OUT
- net 3.3V: now also BAT3.+, C23.1, J1.VDD, J2.VDD, R29.1, R39.1, R42.2, U1.+VS, U1.FR, U2.VDD, U4.VDD; no longer C31.1, C32.1, CONN5.2, U$2.LED, U$5.VCC, U3.OUT
- net GND: now also BAT3.-, C22.2, J1.VSS(GND), J2.VSS(GND), R36.1, R41.1, U1.GND_PAD, U2.GND@2, U2.GND@3, U2.GND@4, U4.GND@2, U4.GND@3, U4.GND@4; no longer BATT.1, C21.2, C22.1, C24.2, C25.2, C26.2, C27.2, C28.2, C29.2, C30.2, C31.2, C32.2, C33.2, C34.2, C35.2, C36.1, C37.2, C38.1, C39.2, C40.2, C41.2, C42.2, C43.2, C44.2, CONN3.7, CONN4.7, CONN5.4, CONN5.5, D13.C, D13_2.C, FET1.S, FET3.S, JP3.6, JP4.6, MINIUSB1G$1.5, MINIUSB1S.S1, MINIUSB1S.S2, MINIUSB1S.S3, MINIUSB1S.S4, MINIUSBG$1.5, MINIUSBS.S1, MINIUSBS.S2, MINIUSBS.S3, MINIUSBS.S4, R31.2, R42.2, R48.2, R51.1, S1.1, S1.2, S2.1, S2.2, SERVO1(USONIC).1, SERVO2(GRIP).1, SERVO3(GRIPROT).1, SHIFT1A.G, SHIFT1P.GND, SHIFT2A.G, SHIFT2P.GND, STEPPER_DRIVER.9, U$10.GND, U$2.GND, U$3.GND, U$4.GND, U$5.GND, U1.GND1, U1.GND2, U1.GND3, U1.UGND, U2.GND1, U2.GND2, U2.GND3, U2.UGND, U3.GND, U5.VSS, ULTRASONIC.1
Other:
- note added: "Note: Cardiac Monitor Config"
- note removed: "1.8" SPI Display (128*160px)"
- note removed: "3.3V LDO"
- note removed: "38KHz with digital output"
- note removed: "Accelerometer and Gyroscope (GY-521, optional, plug-in module)"
- note removed: "Analog Supply (CPU 1 and CPU 2)"
- note removed: "Arduino Breakouts (CPU 1)"
- note removed: "CPU 1 (ATMEGA32U4)"
- note removed: "CPU 2 (ATMEGA32U4)"
- note removed: "Compass (optional, plug-in module)"
- note removed: "Edubot V.0.12 by Sebastian Muszytowski <muzy@muzy.eu>"
- note removed: "GRIP mechanism servo"
- note removed: "HC-SR04"
- note removed: "HMC5883L"
- note removed: "I2C Pullup"
- note removed: "IR Reciever"
- note removed: "ISP (CPU1)"
- note removed: "ISP (CPU2)"
- note removed: "Infrared Sensors (for Line Following)"
- note removed: "Left Motor"
- note removed: "LiPo Charge Circuit (PROG = 2K = 500mA)"
- note removed: "MPU 6050"
- note removed: "NO SUPPORT FOR VIN DUE TO MISSING REGULATOR. EVERYTHING ABOVE 5.5V DAMAGES THE BOARD!"
- note removed: "NRF24L01 Breakout"
- note removed: "Power Selector"
- note removed: "ROTATE mechanism servo"
- note removed: "Reset (CPU1)"
- note removed: "Reset (CPU2)"
- note removed: "Right Motor"
- note removed: "Servo 1 (Ultrasonic)"
- note removed: "Servo 2 and 3 (Gripper)"
- note removed: "Shift Register and Mulitplexer (CPU 2)"
- note removed: "Status LEDs (CPU1)"
- note removed: "Status LEDs (CPU2)"
- note removed: "Step-Up-Converter (2.8 to 4.2Volt to 5V @ 1A)"
- note removed: "USB (CPU1)"
- note removed: "USB (CPU2)"
- note removed: "Ultrasonic distance sensor"
- note removed: "based on Vinciduino Schematic and ATmega32U4 data sheet; Arduino Leonardo compatible with Headers The user mainly programs this microcontroller."
- note removed: "based on Vinciduino Schematic and ATmega32U4 data sheet; Arduino Leonardo compatible without Headers This microcontroller serves as the "brain" interfacing internal components."
- note removed: "for moving the Ultrasonic distance sensor to scan the environment"
- note removed: "licensed under CC-BY-SA 3.0, based on the beautiful Vinciduino (vinciduino.org), inspired by Sparki (arcbotics.com), made with the lovely Arduino Leonardo in mind (arduino.cc)"
- note removed: "on 2x4pin header pinout"
- note removed: "optional, only populate when no other component provides pullup resistors! Values may vary (from 2.2K to 10K)"
- note removed: "with SD Card Adapter (optional, plug-in module)"
- moved on the sheet: C21, C22, C23, C24, C25, C26, C27

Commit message: Completed Schematic
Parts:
- removed BAT3: 2032, SMTU-2032-1:2032
- removed C21: 1nF, SparkFun-Passives:CAP0603-CAP
- removed C22: 0.1uf, SparkFun-Passives:CAP0603-CAP
- removed C23: 0.1uF, SparkFun-Passives:CAP0603-CAP
- removed C24, C25: 0.33uF, SparkFun-Passives:CAP0805
- removed C26: 1.5nF, SparkFun-Passives:CAP0603-CAP
- removed C27: 10nF, SparkFun-Passives:CAP0603-CAP
- removed J1: (no value), tag-connect:TC2030-MCP-NL
- removed JP3, JP4: SEWTAP2, LilyPad-Wearables:SEWTAP2
- removed LOGO3: OSHW-LOGOS, SparkFun-Aesthetics:OSHW-LOGOS
- removed R25, R26: 180k, SparkFun-Passives:RESISTOR0603-RES
- removed R27, R30, R37: 1M, SparkFun-Passives:RESISTOR0603-RES
- removed R28, R29, R32, R33, R35, R36: 10M, SparkFun-Passives:RESISTOR0603-RES
- removed R31: 100k, SparkFun-Passives:RESISTOR0603-RES
- removed R34: 1.4M, SparkFun-Passives:RESISTOR0603-RES
- removed R38: 360k, SparkFun-Passives:RESISTOR0603-RES
- removed R39, R41: 0, SparkFun-Resistors:0OHM1/10W5%(0603)
- removed R40, R42: DNP, SparkFun-Resistors:0OHM1/10W5%(0603)
- removed U1: AD8232, AD8232:AD8232
- removed U4: BGM111-VISUAL-A, sf-bluegiga:BGM111-VISUAL-A
- added JP5: (no value), jumper:JP1E
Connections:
- removed net 3.3V: BAT3.+, C23.1, J1.VDD, J2.VDD, R29.1, R39.1, R42.2, U1.+VS, U1.FR, U2.VDD, U4.VDD
- removed net LA: JP3.1, R25.1, R33.1
- removed net LO+: U1.LO+
- removed net LO-: U1.LO-
- removed net N$100: C24.1, R34.2, R40.2, U1.SW
- removed net N$101: C21.1, U1.RLDFB
- removed net N$102: C26.2, R27.1, R37.1
- removed net N$103: C21.2, R38.1, U1.RLD
- removed net N$104: R35.1, R37.2, U1.IAOUT
- removed net N$105: R32.2, R33.2, R39.2, R40.1
- removed net N$106: R41.2, R42.1, U1.AC/!DC
- removed net N$107: J1.VPP/MCLR, U4.RESET
- removed net N$108: J1.ICSP_CLK/PGC, U4.PF0
- removed net N$109: J1.ICSP_DAT/PGD, U4.PF1
- removed net N$92: R25.2, U1.+IN
- removed net N$93: R26.2, U1.-IN
- removed net N$94: C27.2, R27.2, U1.OPAMP+
- removed net N$95: C25.2, R28.1, U1.HPSENSE
- removed net N$96: C22.1, R29.2, R36.2, U1.REFIN
- removed net N$97: R30.2, R31.1, U1.OPAMP-
- removed net N$98: C25.1, U1.HPDRIVE
- removed net N$99: R28.2, R34.1, R35.2
- removed net RA: JP4.1, R26.1, R32.1
- removed net REFOUT: C24.2, C27.1, R31.2, U1.REFOUT
- removed net RL: R38.2
- removed net SDN: U1.!SDN
- removed net SIGNAL_OUT: C26.1, R30.1, U1.OUT
- new net VAA: BAT1.+, C1.2, C10.2, C11.2, C18.2, C2.2, C4.2, C45.2, C5.2, C7.2, C8.2, IA_1.+VS, IA_1.BW, IA_2.+VS, IA_2.BW, IA_3.+VS, IA_3.BW, IA_4.+VS, IA_4.BW, IC1.V-, IC11P.V+, IC2.V-, IC3.V-, IC4.V-, IC6.AVDD, IC6.DVDD, JP5.1
- net GND: now also JP5.2; no longer BAT3.-, C22.2, C23.2, J1.VSS(GND), R36.1, R41.1, U1.GND, U1.GND_PAD, U4.GND, U4.GND@2, U4.GND@3, U4.GND@4
- net N$11: now also R23.1
- net N$13: now also R13.1
- net N$22: now also R22.1
- net VDD: now also J2.VDD, U2.VDD; no longer BAT1.+, C1.2, C10.2, C11.2, C18.2, C2.2, C4.2, C45.2, C5.2, C7.2, C8.2, IA_1.+VS, IA_1.BW, IA_2.+VS, IA_2.BW, IA_3.+VS, IA_3.BW, IA_4.+VS, IA_4.BW, IC1.V-, IC11P.V+, IC2.V-, IC3.V-, IC4.V-, IC6.AVDD, IC6.DVDD
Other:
- note removed: "Note: Cardiac Monitor Config"
